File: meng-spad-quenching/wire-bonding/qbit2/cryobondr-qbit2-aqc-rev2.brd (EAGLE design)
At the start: 40 x 36 mm, 13 parts, among them IC1 QBIT2-WIREBOND-CRYO1, X1 CONN-D3, X2 CONN-D5, X3 CONN-D4, X4 CONN-D2, X5 CONN-D1, X6 CONN-D6, X7 CONN-D7, X8 CONN-D8

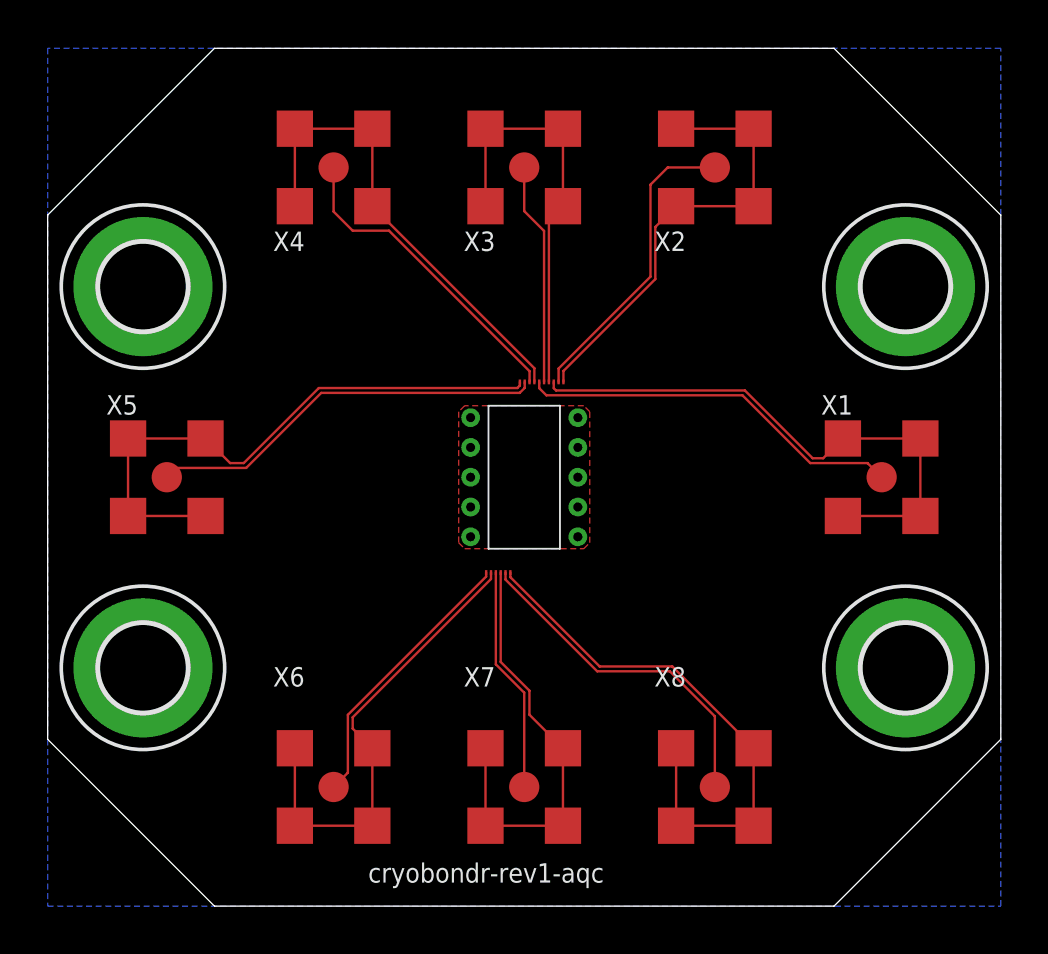
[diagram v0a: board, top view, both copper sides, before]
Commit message: Added TVS diodes to all SPADs, grounded all anodes
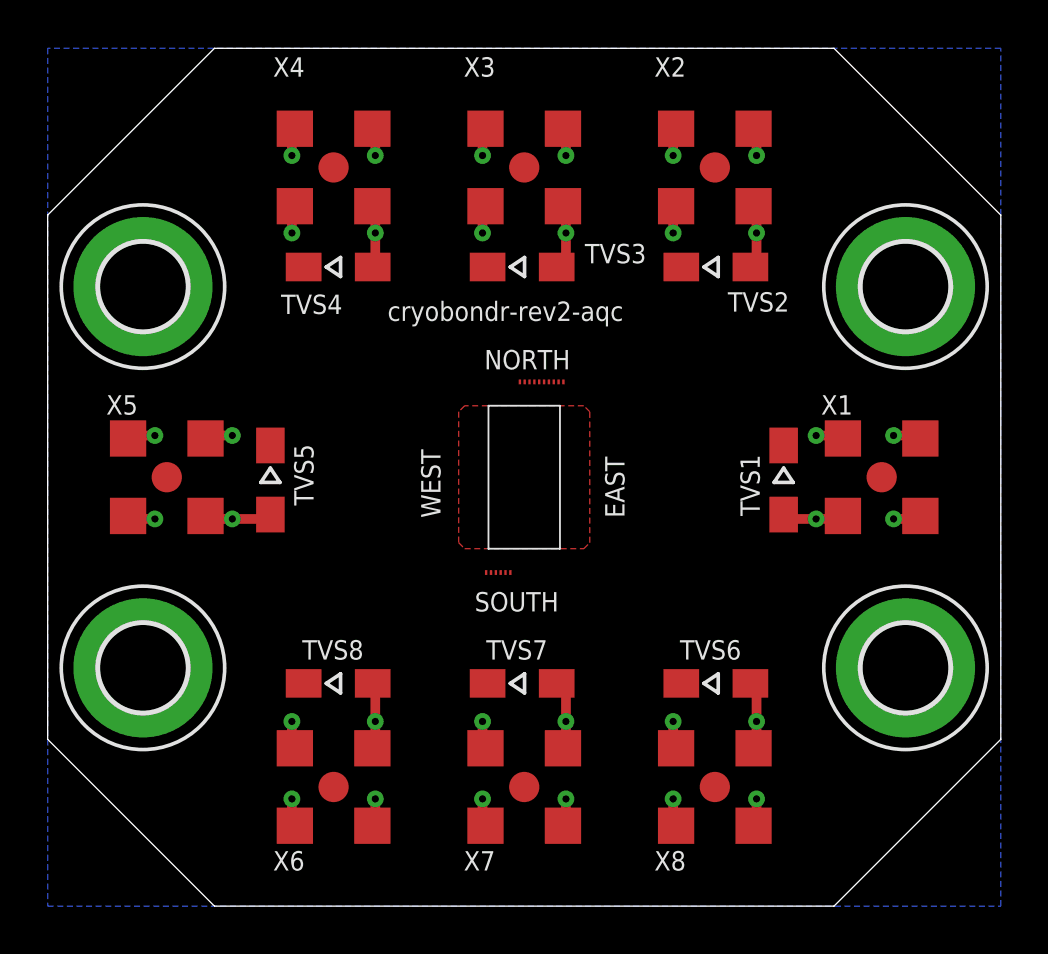
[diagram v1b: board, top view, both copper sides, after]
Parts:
- added TVS1, TVS2, TVS3, TVS4, TVS5, TVS6, TVS7, TVS8: DF2B36FU,H3F, diode:SOD323-W
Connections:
- removed net D1-P-ANODE: IC1.D1-P-ANODE, X5.G1, X5.G2, X5.G3, X5.G4
- removed net D2-P-ANODE: IC1.D2-P-ANODE, X4.G1, X4.G2, X4.G3, X4.G4
- removed net D3-P-ANODE: IC1.D3-P-ANODE, X1.G1, X1.G2, X1.G3, X1.G4
- removed net D4-P-ANODE: IC1.D4-P-ANODE, X3.G1, X3.G2, X3.G3, X3.G4
- removed net D5-P-ANODE: IC1.D5-P-ANODE, X2.G1, X2.G2, X2.G3, X2.G4
- removed net D6-P-ANODE: IC1.D6-P-ANODE, X6.G1, X6.G2, X6.G3, X6.G4
- removed net D7-P-ANODE: IC1.D7-P-ANODE, X7.G1, X7.G2, X7.G3, X7.G4
- removed net D8-P-ANODE: IC1.D8-P-ANODE, X8.G1, X8.G2, X8.G3, X8.G4
- net D1-N-CATHODE: now also TVS5.C
- net D2-N-CATHODE: now also TVS4.C
- net D3-N-CATHODE: now also TVS1.C
- net D4-N-CATHODE: now also TVS3.C
- net D5-N-CATHODE: now also TVS2.C
- net D6-N-CATHODE: now also TVS8.C
- net D7-N-CATHODE: now also TVS7.C
- net D8-N-CATHODE: now also TVS6.C
- net GND: now also IC1.D1-P-ANODE, IC1.D2-P-ANODE, IC1.D3-P-ANODE, IC1.D4-P-ANODE, IC1.D5-P-ANODE, IC1.D6-P-ANODE, IC1.D7-P-ANODE, IC1.D8-P-ANODE, TVS1.A, TVS2.A, TVS3.A, TVS4.A, TVS5.A, TVS6.A, TVS7.A, TVS8.A, X1.G1, X1.G2, X1.G3, X1.G4, X2.G1, X2.G2, X2.G3, X2.G4, X3.G1, X3.G2, X3.G3, X3.G4, X4.G1, X4.G2, X4.G3, X4.G4, X5.G1, X5.G2, X5.G3, X5.G4, X6.G1, X6.G2, X6.G3, X6.G4, X7.G1, X7.G2, X7.G3, X7.G4, X8.G1, X8.G2, X8.G3, X8.G4
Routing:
- net GND: track 0.00 -> 50.5 mm, vias 10 -> 32
- net D1-P-ANODE: track 24.9 -> 0.00 mm
- net D3-P-ANODE: track 23.7 -> 0.00 mm
- net D8-P-ANODE: track 23.1 -> 0.00 mm
- net D5-P-ANODE: track 20.2 -> 0.00 mm
- net D2-P-ANODE: track 19.9 -> 0.00 mm
- net D6-P-ANODE: track 19.9 -> 0.00 mm
- net D7-P-ANODE: track 18.2 -> 0.00 mm
- net D4-P-ANODE: track 17.7 -> 0.00 mm
- net D1-N-CATHODE: track 16.8 -> 0.00 mm
- net D3-N-CATHODE: track 16.2 -> 0.00 mm
- net D8-N-CATHODE: track 14.4 -> 0.00 mm
- net D2-N-CATHODE: track 13.3 -> 0.00 mm
- net D5-N-CATHODE: track 12.9 -> 0.00 mm
- net D6-N-CATHODE: track 11.7 -> 0.00 mm
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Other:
- board text added: "EAST"
- board text added: "NORTH"
- board text added: "SOUTH"
- board text added: "WEST"
- board text added: "cryobondr-rev2-aqc"
- board text removed: "cryobondr-rev1-aqc"

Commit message: work on wirebonding board
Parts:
- IC1: value QBIT2-WIREBOND-CRYO1 -> QBIT2-WIREBOND-CRYO2; device meng:QBIT2-WIREBOND-CRYO1 -> meng:QBIT2-WIREBOND-CRYO2
- TVS1, TVS2, TVS3, TVS4, TVS5, TVS7, TVS8: device diode:SOD323-W -> diode:SOD323-R
- X1: value CONN-D3 -> CONN-D1
- X2: value CONN-D5 -> CONN-D2
- X3: value CONN-D4 -> CONN-D3
- X4: value CONN-D2 -> CONN-D4
- X5: value CONN-D1 -> CONN-D5
- moved X1 30.0 mm to (5.00, 18.0)
- moved X5 30.0 mm to (35.0, 18.0), turned to 270 degrees
- moved TVS1 21.5 mm to (9.35, 17.9)
- moved TVS5 21.5 mm to (30.8, 18.0)
- moved X2 16.0 mm to (12.0, 31.0)
- moved X4 16.0 mm to (28.0, 31.0)
- moved TVS2 15.8 mm to (12.2, 26.8)
- moved TVS6 15.8 mm to (12.2, 9.35)
- moved TVS8 15.8 mm to (28.0, 9.35)
- moved TVS4 15.7 mm to (27.9, 26.8)
- moved TVS3 0.21 mm to (20.1, 26.9)
- turned X3 to 90 degrees
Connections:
- net D1-N-CATHODE: now also TVS1.C, X1.S; no longer TVS5.C, X5.S
- net D2-N-CATHODE: now also TVS2.C, X2.S; no longer TVS4.C, X4.S
- net D3-N-CATHODE: now also TVS3.C, X3.S; no longer TVS1.C, X1.S
- net D4-N-CATHODE: now also TVS4.C, X4.S; no longer TVS3.C, X3.S
- net D5-N-CATHODE: now also TVS5.C, X5.S; no longer TVS2.C, X2.S
- net D6-N-CATHODE: now also TVS6.C; no longer TVS8.C
- net D8-N-CATHODE: now also TVS8.C; no longer TVS6.C
- net GND: now also IC1.VSS_BOTTOM, IC1.VSS_TOP
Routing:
- net GND: track 50.5 -> 93.1 mm, vias 32 -> 44
- net D1-N-CATHODE: track 0.00 -> 16.5 mm
- net D5-N-CATHODE: track 0.00 -> 15.8 mm
- net D2-N-CATHODE: track 0.00 -> 15.6 mm
- net D6-N-CATHODE: track 0.00 -> 14.4 mm
- net D8-N-CATHODE: track 0.00 -> 14.2 mm
- net D4-N-CATHODE: track 0.00 -> 13.2 mm
- net D3-N-CATHODE: track 0.00 -> 10.6 mm
- net D7-N-CATHODE: track 0.00 -> 10.1 mm

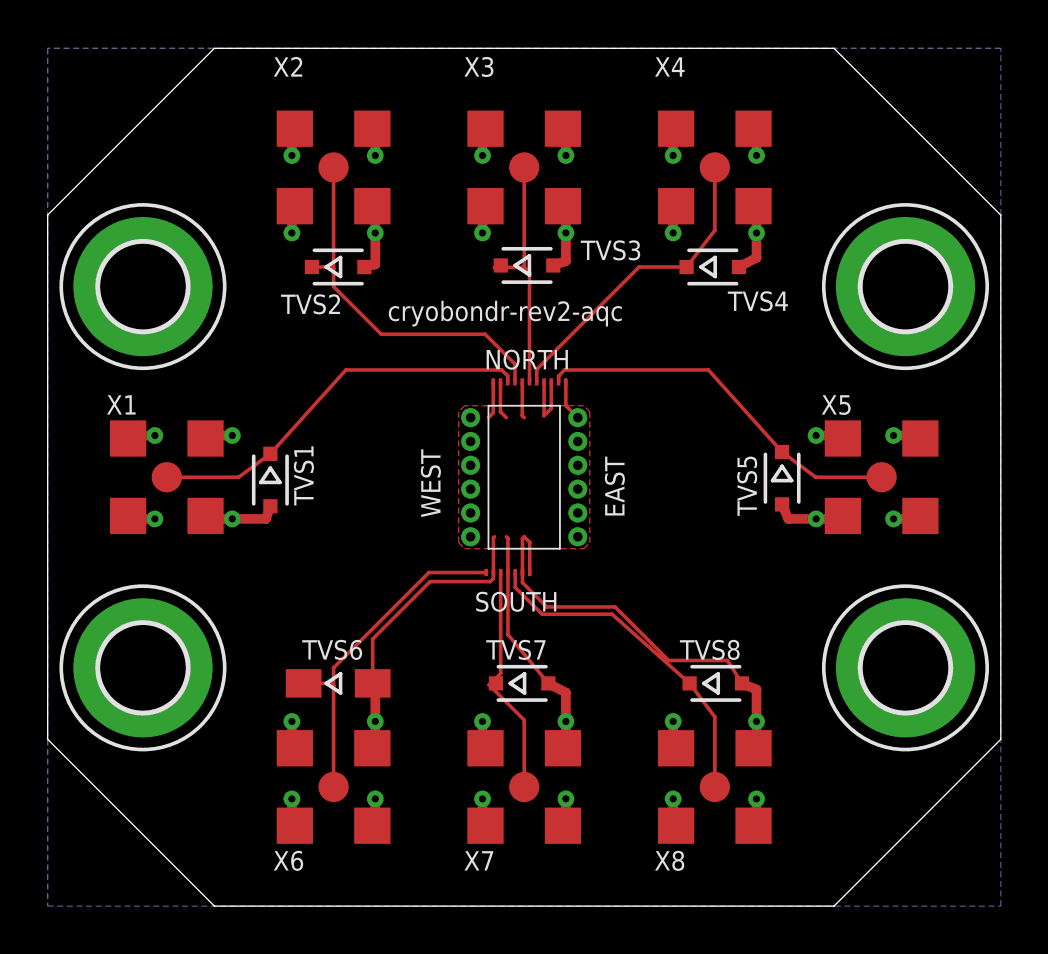
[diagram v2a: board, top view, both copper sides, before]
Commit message: Added plotter to leaf heater system class
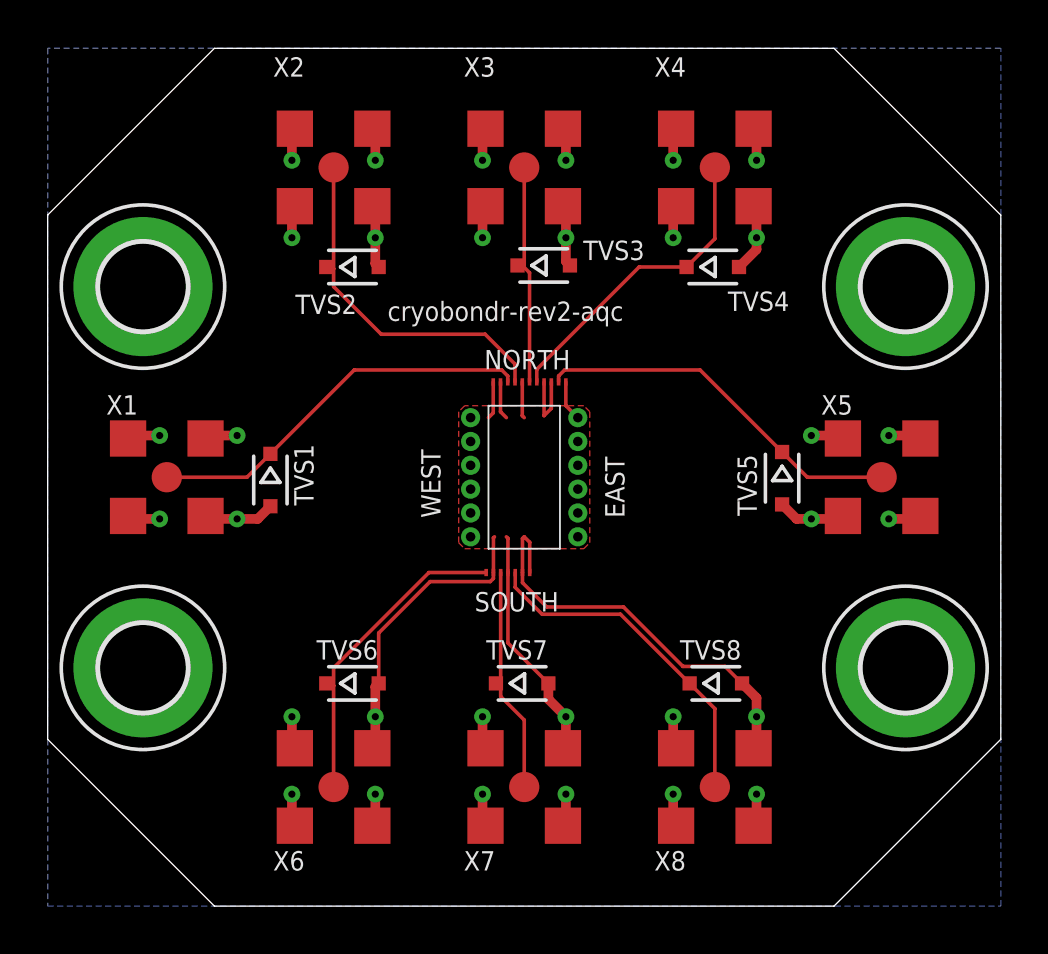
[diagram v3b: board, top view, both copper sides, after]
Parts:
- TVS6: device diode:SOD323-W -> diode:SOD323-R
- moved TVS3 0.70 mm to (20.8, 26.9)
- moved TVS2 0.60 mm to (12.8, 26.8)
- moved TVS6 0.60 mm to (12.8, 9.35)
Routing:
- net GND: track 93.1 -> 96.4 mm
- net D3-N-CATHODE: track 10.6 -> 9.41 mm
- net D6-N-CATHODE: track 14.4 -> 13.4 mm
- net D2-N-CATHODE: track 15.6 -> 15.0 mm
